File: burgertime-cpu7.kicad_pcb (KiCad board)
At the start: 2 copper layers, 80 x 83.1 mm, 20 parts, among them IC1 74LS245, IC10 74LS74, IC2 74LS368, IC3 74LS245, IC4 74LS244, IC5 6502, IC6 74LS367, IC7 74LS244, IC8 74LS10, IC9 74LS00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

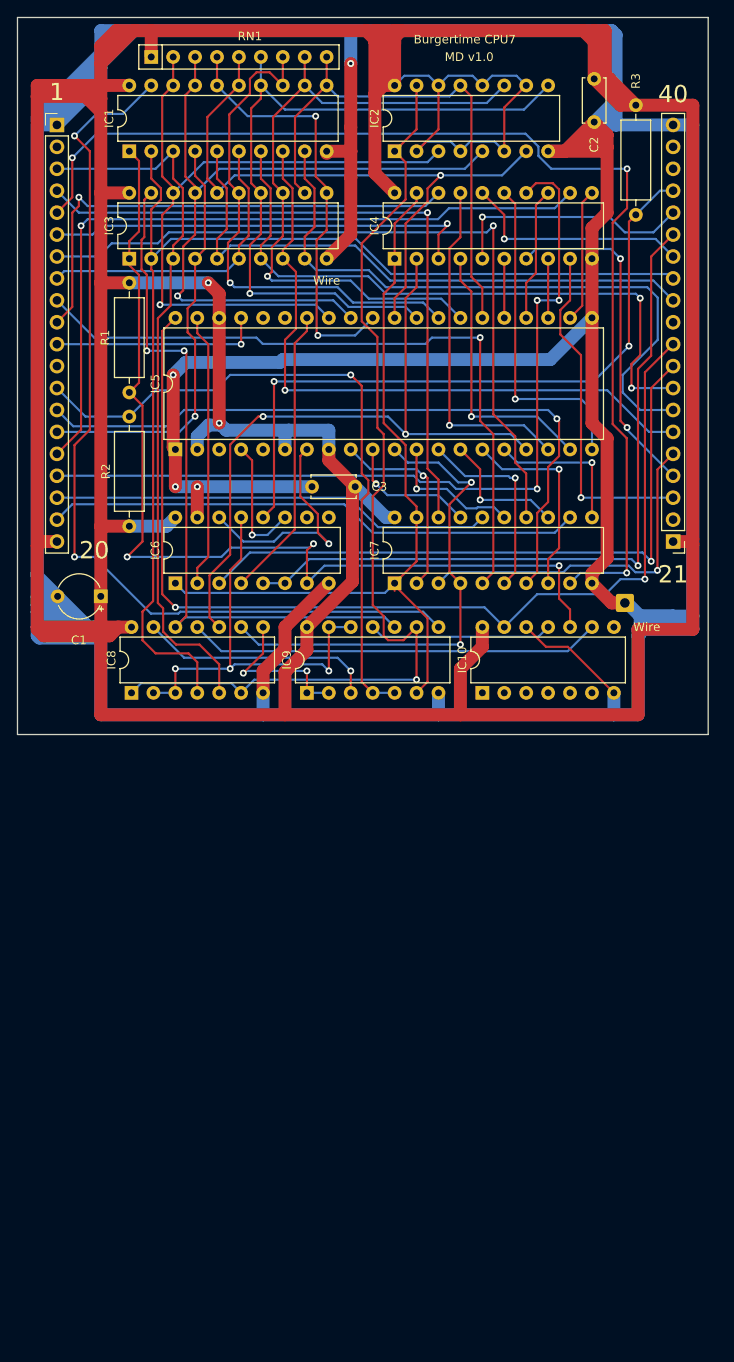
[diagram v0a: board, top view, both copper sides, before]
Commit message: added docs, gerbers, and component values to silkscreen
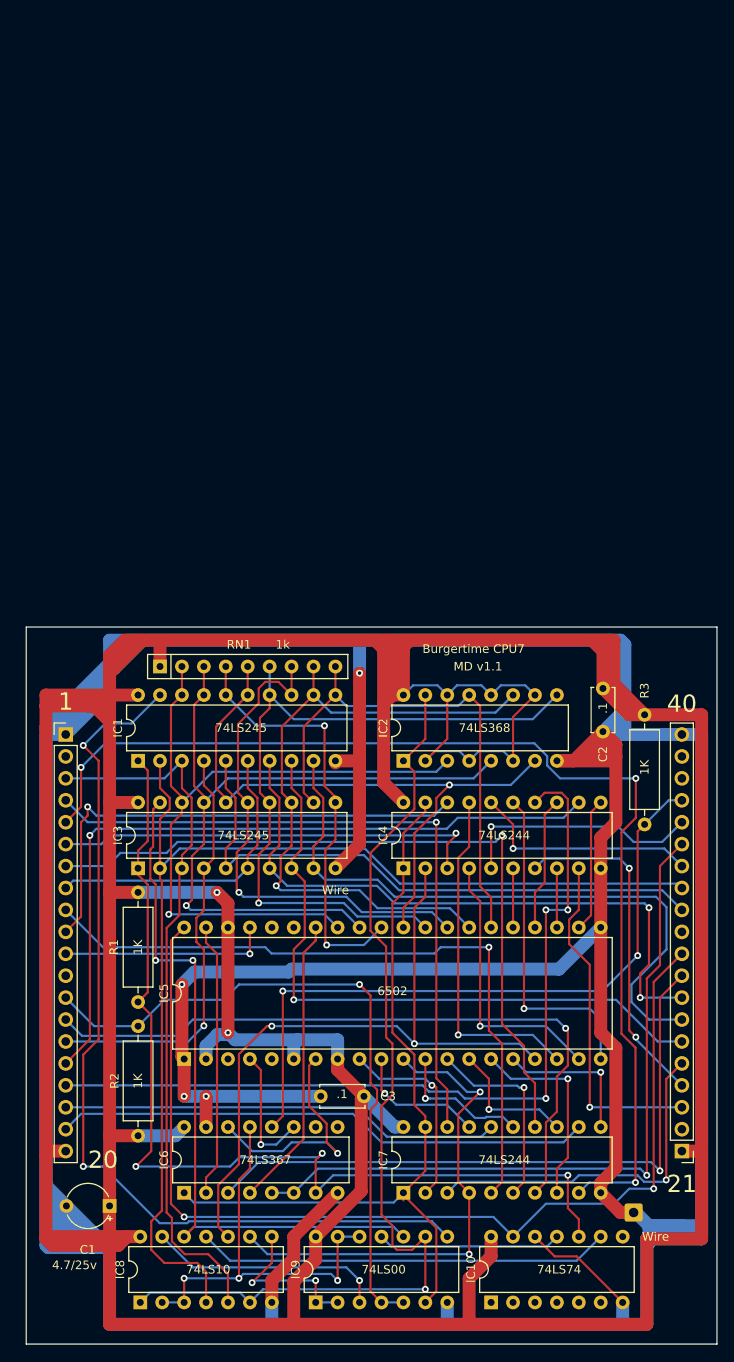
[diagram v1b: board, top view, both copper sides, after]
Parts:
- moved IC10 70.6 mm to (156.5, 133.6)
- moved IC8 70.6 mm to (115.8, 133.6)
- moved IC9 70.6 mm to (136.1, 133.6)
- moved C1 70.6 mm to (112.3, 122.4)
- moved C2 70.6 mm to (169.4, 62.5)
- moved C3 70.6 mm to (141.7, 109.7)
- moved IC1 70.6 mm to (115.6, 70.9)
- moved IC2 70.6 mm to (146.3, 70.9)
- moved IC3 70.6 mm to (115.6, 83.3)
- moved IC4 70.6 mm to (146.3, 83.3)
- moved IC5 70.6 mm to (120.9, 105.4)
- moved IC6 70.6 mm to (120.9, 120.9)
- moved IC7 70.6 mm to (146.3, 120.9)
- moved J1 70.6 mm to (107.2, 67.8)
- moved J2 70.6 mm to (178.6, 116.1)
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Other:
- board text added: "MD v1.1"
- board text removed: "MD v1.0"
